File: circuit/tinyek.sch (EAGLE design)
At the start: 13 parts, among them IC1 ATTiny13A, Q1 2N7000

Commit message: update
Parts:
- added ZD1, ZD2: 5V, diode:ZPD
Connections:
- net GND: now also ZD1.A, ZD2.A
- net N$10: now also ZD1.C
- net N$8: now also ZD2.C
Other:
- moved on the sheet: INPUT, R3, R4

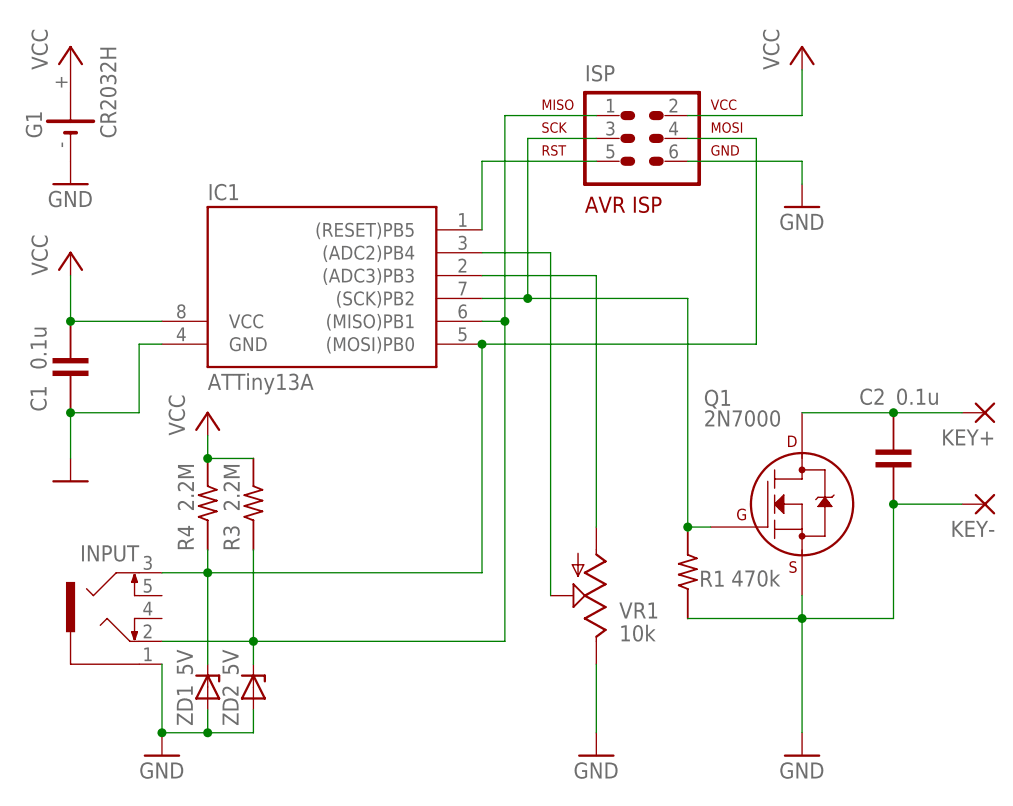
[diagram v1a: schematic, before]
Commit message: 電流制限抵抗を追加
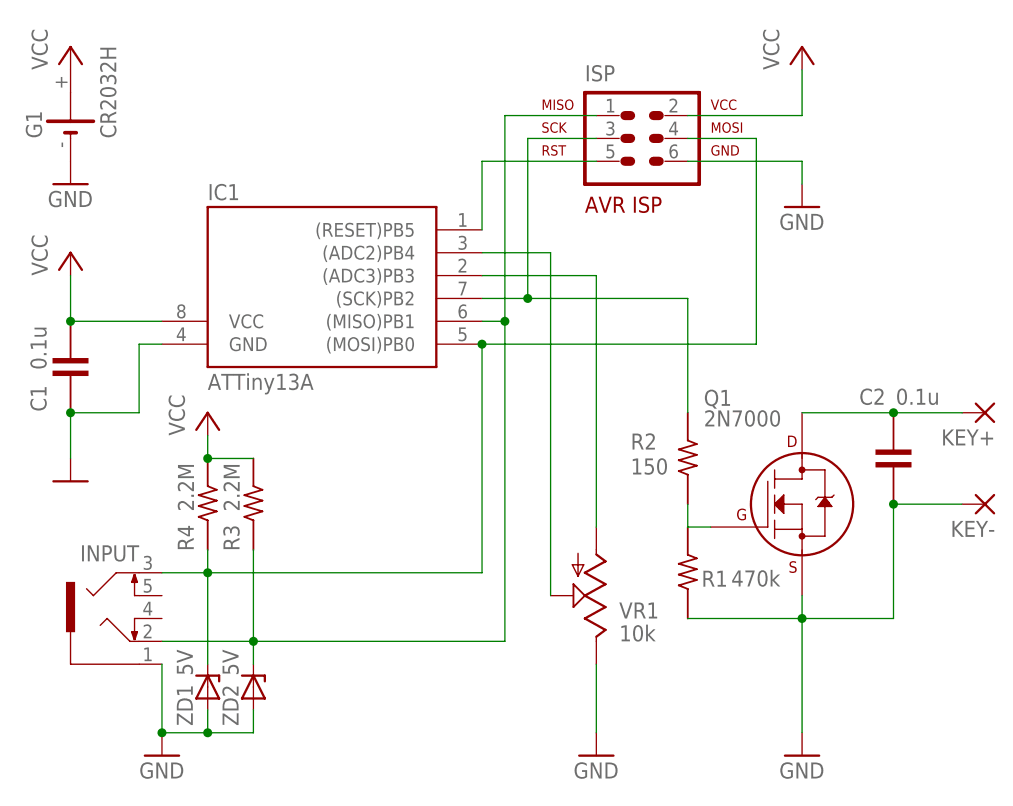
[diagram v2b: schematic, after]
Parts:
- added R2: 150, r-j:R-1/4W-02.54-V
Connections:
- new net N$8: Q1.G, R1.1, R2.2
- net N$4: now also R2.1; no longer Q1.G, R1.1
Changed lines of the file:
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@@
 <layer number="96" name="Values" color="7" fill="1" visible="yes" active="yes"/>
 <layer number="97" name="Info" color="7" fill="1" visible="yes" active="yes"/>
-<layer number="98" name="Guide" color="6" fill="1" visible="no" active="yes"/>
+<layer number="98" name="Guide" color="6" fill="1" visible="yes" active="yes"/>
 <layer number="200" name="200bmp" color="1" fill="10" visible="no" active="no"/>
 </layers>
@@
 <part name="ZD1" library="diode" deviceset="ZPD" device="" value="5V"/>
 <part name="ZD2" library="diode" deviceset="ZPD" device="" value="5V"/>
+<part name="R2" library="r-j" deviceset="R-" device="1/4W-02.54-V" value="150"/>
 </parts>
 <sheets>
@@
 </instance>
 <instance part="R1" gate="R" x="50.8" y="43.18" smashed="yes" rot="R270">
-<attribute name="NAME" x="52.07" y="41.6306" size="1.778" layer="95"/>
+<attribute name="NAME" x="52.324" y="41.6306" size="1.778" layer="95"/>
 <attribute name="VALUE" x="55.626" y="41.656" size="1.778" layer="96"/>
 </instance>
@@
 <attribute name="NAME" x="0.889" y="26.162" size="1.778" layer="95" rot="R90"/>
 <attribute name="VALUE" x="0.889" y="31.75" size="1.778" layer="96" rot="R90"/>
+</instance>
+<instance part="R2" gate="R" x="50.8" y="55.88" smashed="yes" rot="R270">
+<attribute name="NAME" x="44.45" y="56.8706" size="1.778" layer="95"/>
+<attribute name="VALUE" x="44.45" y="54.102" size="1.778" layer="96"/>
 </instance>
 </instances>
@@
 <net name="N$4" class="0">
 <segment>
-<pinref part="Q1" gate="G$1" pin="G"/>
-<wire x1="53.34" y1="48.26" x2="50.8" y2="48.26" width="0.1524" layer="91"/>
-<pinref part="R1" gate="R" pin="1"/>
-<junction x="50.8" y="48.26"/>
 <pinref part="IC1" gate="G$1" pin="(SCK)PB2"/>
-<wire x1="50.8" y1="48.26" x2="50.8" y2="73.66" width="0.1524" layer="91"/>
 <wire x1="50.8" y1="73.66" x2="33.02" y2="73.66" width="0.1524" layer="91"/>
 <pinref part="ISP" gate="G$1" pin="3"/>
@@
 <wire x1="33.02" y1="91.44" x2="33.02" y2="73.66" width="0.1524" layer="91"/>
 <junction x="33.02" y="73.66"/>
+<pinref part="R2" gate="R" pin="1"/>
+<wire x1="50.8" y1="60.96" x2="50.8" y2="73.66" width="0.1524" layer="91"/>
 </segment>
 </net>
@@
 </segment>
 </net>
-<net name="N$8" class="0">
+<net name="N$11" class="0">
 <segment>
 <pinref part="INPUT" gate="G$1" pin="2"/>
@@
 </segment>
 </net>
+<net name="N$8" class="0">
+<segment>
+<pinref part="Q1" gate="G$1" pin="G"/>
+<wire x1="53.34" y1="48.26" x2="50.8" y2="48.26" width="0.1524" layer="91"/>
+<pinref part="R1" gate="R" pin="1"/>
+<pinref part="R2" gate="R" pin="2"/>
+<wire x1="50.8" y1="48.26" x2="50.8" y2="50.8" width="0.1524" layer="91"/>
+</segment>
+</net>
